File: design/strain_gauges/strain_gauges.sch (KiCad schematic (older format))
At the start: 32 parts, among them J1 Conn_01x03, J2 Conn_01x03, J3 Conn_01x08, J4 Conn_01x04_swapped, J5 Conn_01x04_swapped, J6 Conn_01x04_swapped, J7 Conn_01x04_swapped, P1 CONN_01X02, Q1 BC640, U1 LT1460-10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

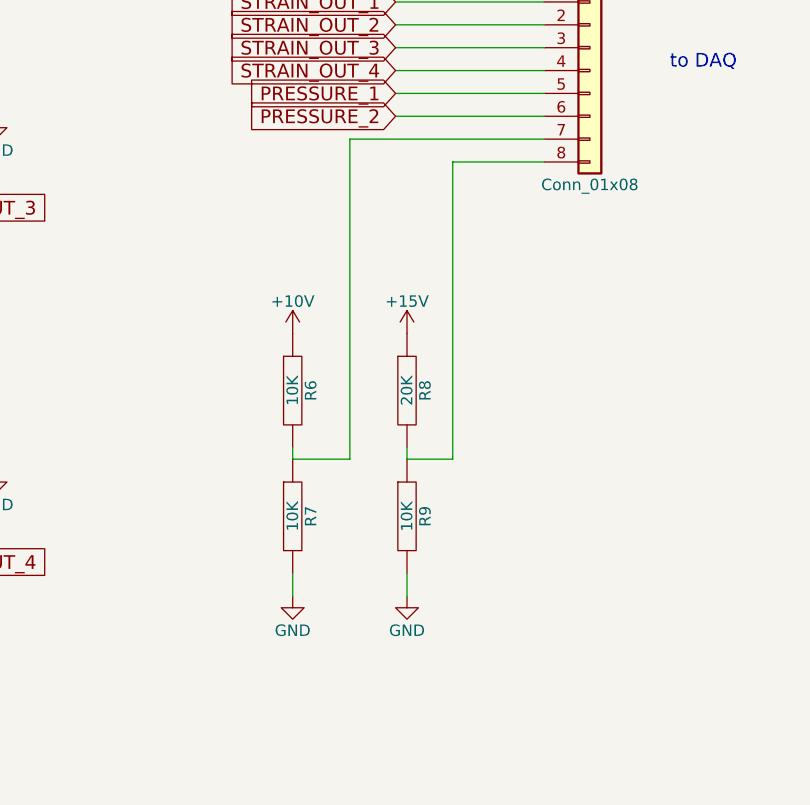
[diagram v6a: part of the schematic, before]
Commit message: Board layout & routing rework
- Move the power blocks further into the board
- ground planing not done yet
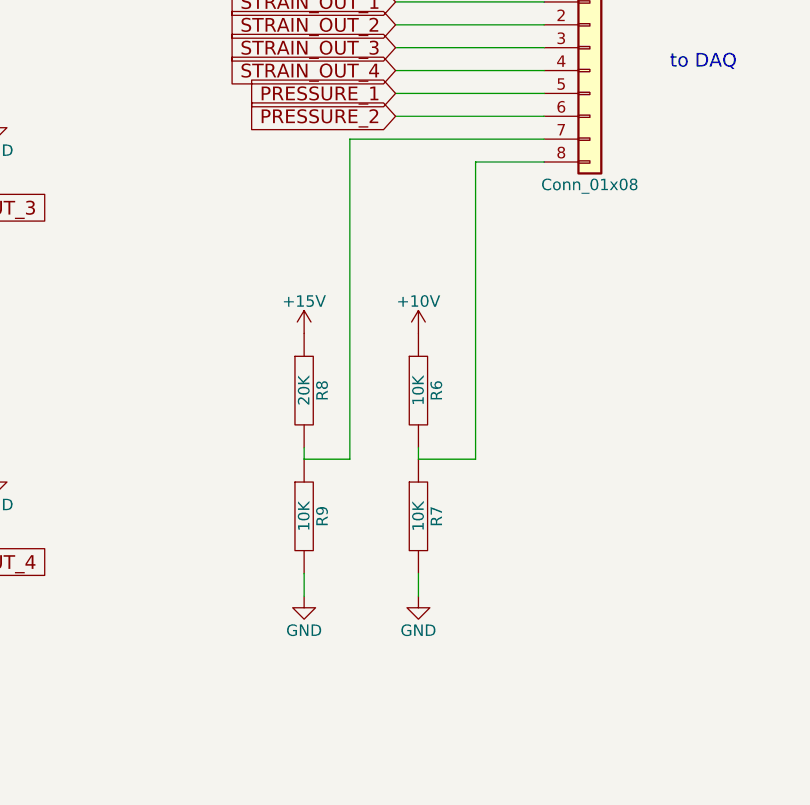
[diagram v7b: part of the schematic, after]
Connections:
- net at R6.2, R7.1: now also J3.8 (Pin_8); no longer J3.7 (Pin_7)
- net at R8.2, R9.1: now also J3.7 (Pin_7); no longer J3.8 (Pin_8)
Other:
- moved on the sheet: R6, R7, R8, R9
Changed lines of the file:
@@
 L +10V #PWR034
 U 1 1 5A4C1972
-P 8300 4600
-F 0 "#PWR034" H 8300 4450 50  0001 C CNN
-F 1 "+10V" H 8300 4740 50  0000 C CNN
-F 2 "" H 8300 4600 50  0000 C CNN
-F 3 "" H 8300 4600 50  0000 C CNN
-	1    8300 4600
+P 8850 4600
+F 0 "#PWR034" H 8850 4450 50  0001 C CNN
+F 1 "+10V" H 8850 4740 50  0000 C CNN
+F 2 "" H 8850 4600 50  0000 C CNN
+F 3 "" H 8850 4600 50  0000 C CNN
+	1    8850 4600
 	1    0    0    -1
 $EndComp
@@
 L R R6
 U 1 1 5A4C19DA
-P 8300 4850
-F 0 "R6" V 8380 4850 50  0000 C CNN
-F 1 "10K" V 8300 4850 50  0000 C CNN
-F 2 "Resistors_SMD:R_0805_HandSoldering" H 8300 4850 50  0001 C CNN
-F 3 "" H 8300 4850 50  0001 C CNN
-	1    8300 4850
+P 8850 4850
+F 0 "R6" V 8930 4850 50  0000 C CNN
+F 1 "10K" V 8850 4850 50  0000 C CNN
+F 2 "Resistors_SMD:R_0805_HandSoldering" H 8850 4850 50  0001 C CNN
+F 3 "" H 8850 4850 50  0001 C CNN
+	1    8850 4850
 	1    0    0    -1
 $EndComp
@@
 L R R7
 U 1 1 5A4C1A4B
-P 8300 5400
-F 0 "R7" V 8380 5400 50  0000 C CNN
-F 1 "10K" V 8300 5400 50  0000 C CNN
-F 2 "Resistors_SMD:R_0805_HandSoldering" H 8300 5400 50  0001 C CNN
-F 3 "" H 8300 5400 50  0001 C CNN
-	1    8300 5400
+P 8850 5400
+F 0 "R7" V 8930 5400 50  0000 C CNN
+F 1 "10K" V 8850 5400 50  0000 C CNN
+F 2 "Resistors_SMD:R_0805_HandSoldering" H 8850 5400 50  0001 C CNN
+F 3 "" H 8850 5400 50  0001 C CNN
+	1    8850 5400
 	1    0    0    -1
 $EndComp
@@
 L GND #PWR035
 U 1 1 5A4C274E
-P 8300 5750
-F 0 "#PWR035" H 8300 5500 50  0001 C CNN
-F 1 "GND" H 8300 5600 50  0000 C CNN
-F 2 "" H 8300 5750 50  0001 C CNN
-F 3 "" H 8300 5750 50  0001 C CNN
-	1    8300 5750
+P 8850 5750
+F 0 "#PWR035" H 8850 5500 50  0001 C CNN
+F 1 "GND" H 8850 5600 50  0000 C CNN
+F 2 "" H 8850 5750 50  0001 C CNN
+F 3 "" H 8850 5750 50  0001 C CNN
+	1    8850 5750
 	1    0    0    -1
 $EndComp
@@
 L R R8
 U 1 1 5A4C2B16
-P 8800 4850
-F 0 "R8" V 8880 4850 50  0000 C CNN
-F 1 "20K" V 8800 4850 50  0000 C CNN
-F 2 "Resistors_SMD:R_0805_HandSoldering" H 8800 4850 50  0001 C CNN
-F 3 "" H 8800 4850 50  0001 C CNN
-	1    8800 4850
+P 8350 4850
+F 0 "R8" V 8430 4850 50  0000 C CNN
+F 1 "20K" V 8350 4850 50  0000 C CNN
+F 2 "Resistors_SMD:R_0805_HandSoldering" H 8350 4850 50  0001 C CNN
+F 3 "" H 8350 4850 50  0001 C CNN
+	1    8350 4850
 	1    0    0    -1
 $EndComp
@@
 L R R9
 U 1 1 5A4C2B1C
-P 8800 5400
-F 0 "R9" V 8880 5400 50  0000 C CNN
-F 1 "10K" V 8800 5400 50  0000 C CNN
-F 2 "Resistors_SMD:R_0805_HandSoldering" H 8800 5400 50  0001 C CNN
-F 3 "" H 8800 5400 50  0001 C CNN
-	1    8800 5400
+P 8350 5400
+F 0 "R9" V 8430 5400 50  0000 C CNN
+F 1 "10K" V 8350 5400 50  0000 C CNN
+F 2 "Resistors_SMD:R_0805_HandSoldering" H 8350 5400 50  0001 C CNN
+F 3 "" H 8350 5400 50  0001 C CNN
+	1    8350 5400
 	1    0    0    -1
 $EndComp
@@
 L GND #PWR036
 U 1 1 5A4C2B23
-P 8800 5750
-F 0 "#PWR036" H 8800 5500 50  0001 C CNN
-F 1 "GND" H 8800 5600 50  0000 C CNN
-F 2 "" H 8800 5750 50  0001 C CNN
-F 3 "" H 8800 5750 50  0001 C CNN
-	1    8800 5750
+P 8350 5750
+F 0 "#PWR036" H 8350 5500 50  0001 C CNN
+F 1 "GND" H 8350 5600 50  0000 C CNN
+F 2 "" H 8350 5750 50  0001 C CNN
+F 3 "" H 8350 5750 50  0001 C CNN
+	1    8350 5750
 	1    0    0    -1
 $EndComp
@@
 L +15V #PWR037
 U 1 1 5A4C2B8F
-P 8800 4600
-F 0 "#PWR037" H 8800 4450 50  0001 C CNN
-F 1 "+15V" H 8800 4740 50  0000 C CNN
-F 2 "" H 8800 4600 50  0000 C CNN
-F 3 "" H 8800 4600 50  0000 C CNN
-	1    8800 4600
+P 8350 4600
+F 0 "#PWR037" H 8350 4450 50  0001 C CNN
+F 1 "+15V" H 8350 4740 50  0000 C CNN
+F 2 "" H 8350 4600 50  0000 C CNN
+F 3 "" H 8350 4600 50  0000 C CNN
+	1    8350 4600
 	1    0    0    -1
 $EndComp
@@
 	5000 5700 5200 5700
 Wire Wire Line
-	8300 5100 8300 5150
-Wire Wire Line
-	8300 5750 8300 5650
-Wire Wire Line
-	8800 5100 8800 5150
-Wire Wire Line
-	8800 5750 8800 5650
-Wire Wire Line
-	8300 5150 8550 5150
-Wire Wire Line
-	8800 5150 9000 5150
+	8850 5100 8850 5150
+Wire Wire Line
+	8850 5750 8850 5650
+Wire Wire Line
+	8350 5100 8350 5150
+Wire Wire Line
+	8350 5750 8350 5650
+Wire Wire Line
+	8850 5150 9100 5150
+Wire Wire Line
+	8350 5150 8550 5150
 Wire Wire Line
 	3150 950  3150 1350
@@
 	2650 2900 2650 2800
 Connection ~ 2650 2800
-Wire Wire Line
-	8550 5150 8550 3750
-Wire Wire Line
-	8550 3750 9400 3750
-Wire Wire Line
-	9000 5150 9000 3850
-Wire Wire Line
-	9000 3850 9400 3850
 Wire Wire Line
 	1400 3900 1650 3900
@@
 	-1   0    0    1
 $EndComp
+Wire Wire Line
+	8550 5150 8550 3750
+Wire Wire Line
+	8550 3750 9400 3750
+Wire Wire Line
+	9100 5150 9100 3850
+Wire Wire Line
+	9100 3850 9400 3850
 $EndSCHEMATC

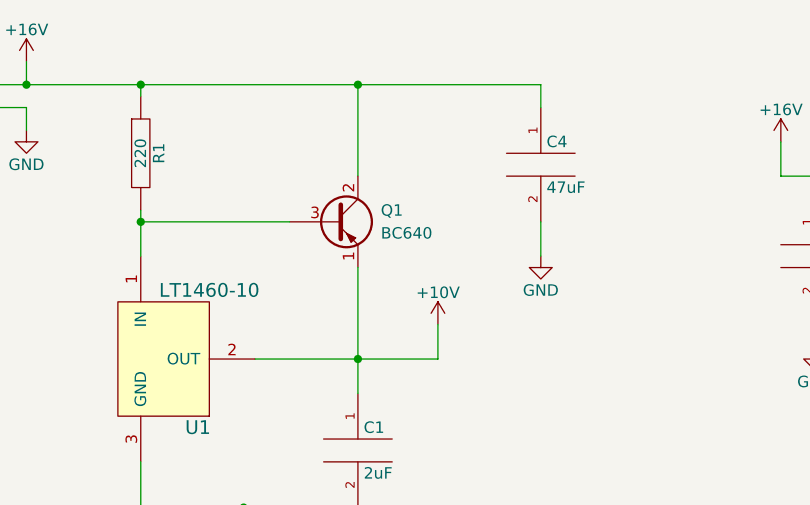
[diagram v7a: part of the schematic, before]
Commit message: Correct PNP orientation in schematic
Also swap out the part for one I have on hand (2N3906)
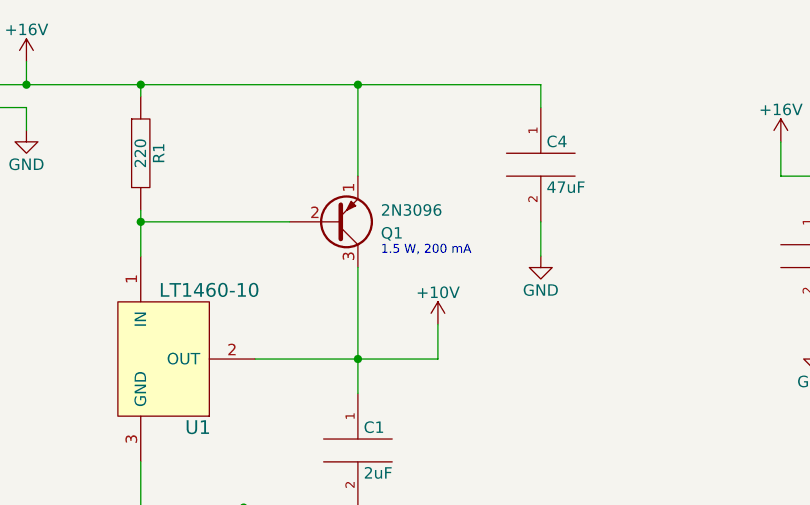
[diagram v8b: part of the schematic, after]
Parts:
- removed Q1: BC640, TO_SOT_Packages_THT:TO-92_Inline_Narrow_Oval, symbol Q_PNP_ECB
- added Q1: 2N3096, TO_SOT_Packages_THT:TO-92_Inline_Narrow_Oval, symbol Q_PNP_EBC
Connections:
- net +10V: now also Q1.3 (C)
- net +16V: now also Q1.1 (E)
- net at R1.2, U1.1 (IN): now also Q1.2 (B)
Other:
- note added: "1.5 W, 200 mA"
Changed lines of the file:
@@
-$EndComp
-$Comp
-L Q_PNP_ECB Q1
-U 1 1 5A4D5BAD
-P 3050 1550
-F 0 "Q1" H 3250 1600 50  0000 L CNN
-F 1 "BC640" H 3250 1500 50  0000 L CNN
-F 2 "TO_SOT_Packages_THT:TO-92_Inline_Narrow_Oval" H 3250 1650 50  0001 C CNN
-F 3 "" H 3050 1550 50  0001 C CNN
-	1    3050 1550
-	1    0    0    -1
 $EndComp
 $Comp
@@
 Wire Wire Line
 	9100 3850 9400 3850
+$Comp
+L Q_PNP_EBC Q1
+U 1 1 5A567EE1
+P 3050 1550
+F 0 "Q1" H 3250 1600 50  0000 L CNN
+F 1 "2N3096" H 3250 1500 50  0000 L CNN
+F 2 "TO_SOT_Packages_THT:TO-92_Inline_Narrow_Oval" H 3250 1650 50  0001 C CNN
+F 3 "" H 3050 1550 50  0001 C CNN
+	1    3050 1550
+	1    0    0    1
+$EndComp
+Text Notes 3250 1700 0    39   ~ 0
+1.5 W, 200 mA
 $EndSCHEMATC
